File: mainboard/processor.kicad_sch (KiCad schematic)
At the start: 83 parts, among them J10 6502, J11 6502, J12 Y, J13 Conn_01x16, J14 NO DMA, J3 EDAC 305-044-520-201, J4 W, J5 X, J6 S, J7 R, J8 T, J9 Z, Q1 Q_NPN_EBC, Q2 Q_PNP_EBC, Q3 Q_NPN_EBC, Q4 Q_PNP_EBC

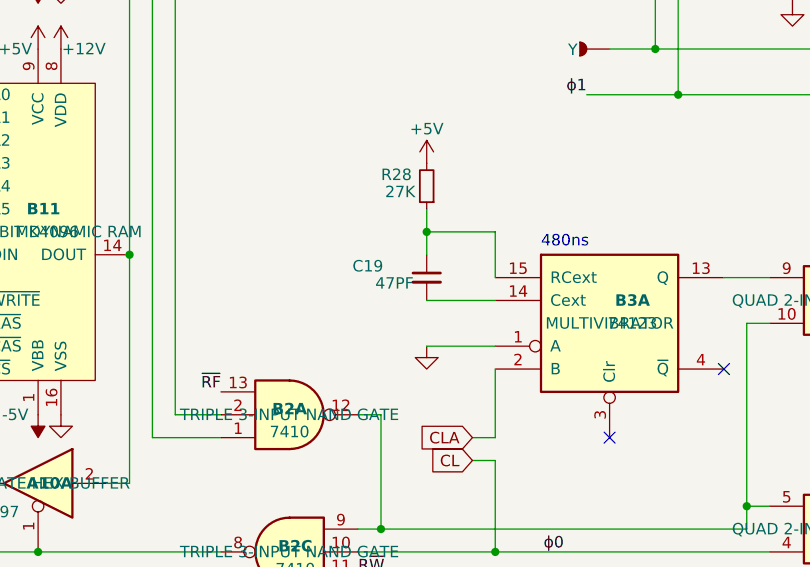
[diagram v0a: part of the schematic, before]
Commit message: added graphicard
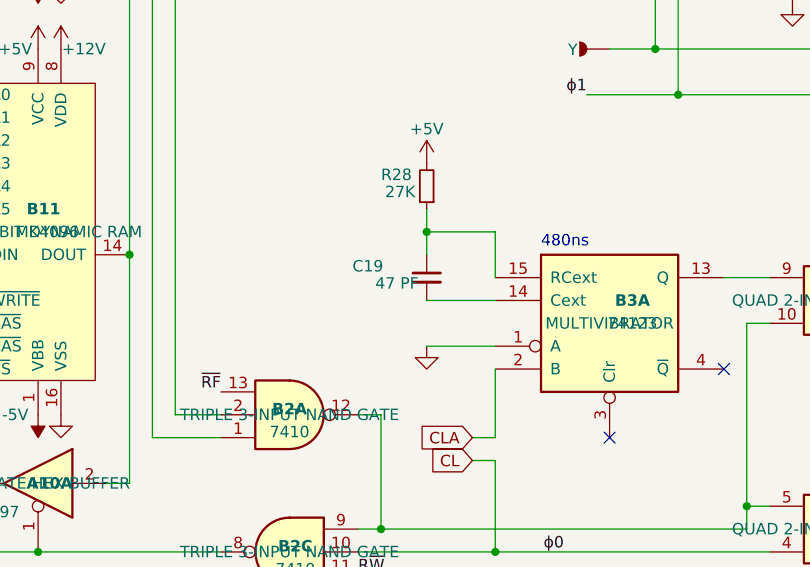
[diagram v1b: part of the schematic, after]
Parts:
- C19: value 47PF -> 47 PF
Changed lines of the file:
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@@
 			)
 		)
-		(property "Value" "47PF"
+		(property "Value" "47 PF"
 			(at 413.385 142.875 0)
 			(show_name no)

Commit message: mainboard work
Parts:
- C10, C11, C12, C13, C8, C9, R16, R17, R18, R19, R20, R21, R22, R23: now not fitted; now left out of the parts list
- C15, C16, C17, C18, C21, C22, C23, C24: footprint mainboard:apple-1_C_Disc_D16.0mm_W5.0mm_P7.50mm -> mainboard:apple-1_C_Disc_D16.0mm_W5.0mm_P275mils
- Q1, Q2, Q3, Q4: now not fitted
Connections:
- net at B3.14 (Cext): now also C19.1; no longer C19.2
- net at B3.15 (RCext), R28.1: now also C19.2; no longer C19.1
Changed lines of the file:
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@@
 		(body_style 1)
 		(exclude_from_sim no)
-		(in_bom yes)
+		(in_bom no)
 		(on_board yes)
 		(in_pos_files yes)
-		(dnp no)
+		(dnp yes)
 		(property "Reference" "C8"
 			(at 248.158 253.238 0)
@@
 		(body_style 1)
 		(exclude_from_sim no)
-		(in_bom yes)
+		(in_bom no)
 		(on_board yes)
 		(in_pos_files yes)
-		(dnp no)
+		(dnp yes)
 		(property "Reference" "C9"
 			(at 248.412 237.998 0)
@@
 		(body_style 1)
 		(exclude_from_sim no)
-		(in_bom yes)
+		(in_bom no)
 		(on_board yes)
 		(in_pos_files yes)
-		(dnp no)
+		(dnp yes)
 		(property "Reference" "R21"
 			(at 259.334 240.284 0)
@@
 		(body_style 1)
 		(exclude_from_sim no)
-		(in_bom yes)
+		(in_bom no)
 		(on_board yes)
 		(in_pos_files yes)
-		(dnp no)
+		(dnp yes)
 		(property "Reference" "R20"
 			(at 259.334 250.444 0)
@@
 		(body_style 1)
 		(exclude_from_sim no)
-		(in_bom yes)
+		(in_bom no)
 		(on_board yes)
 		(in_pos_files yes)
-		(dnp no)
+		(dnp yes)
 		(property "Reference" "R16"
 			(at 247.142 263.144 0)
@@
 		(body_style 1)
 		(exclude_from_sim no)
-		(in_bom yes)
+		(in_bom no)
 		(on_board yes)
 		(in_pos_files yes)
-		(dnp no)
+		(dnp yes)
 		(property "Reference" "R17"
 			(at 247.396 227.838 0)
@@
 		(body_style 1)
 		(exclude_from_sim no)
-		(in_bom yes)
+		(in_bom no)
 		(on_board yes)
 		(in_pos_files yes)
-		(dnp no)
+		(dnp yes)
 		(property "Reference" "C12"
 			(at 261.874 233.426 0)
@@
 		(on_board yes)
 		(in_pos_files yes)
-		(dnp no)
+		(dnp yes)
 		(property "Reference" "Q1"
 			(at 256.54 259.08 0)
@@
 		(on_board yes)
 		(in_pos_files yes)
-		(dnp no)
+		(dnp yes)
 		(property "Reference" "Q2"
 			(at 256.54 233.68 0)
@@
 		(lib_id "Device:C_Small")
 		(at 419.1 142.24 0)
+		(mirror x)
 		(unit 1)
 		(body_style 1)
@@
 		(dnp no)
 		(property "Reference" "C19"
-			(at 410.845 140.97 0)
+			(at 410.845 143.51 0)
 			(show_name no)
 			(do_not_autoplace no)
@@
 		)
 		(property "Value" "47 PF"
-			(at 413.385 142.875 0)
+			(at 413.385 141.605 0)
 			(show_name no)
 			(do_not_autoplace no)
@@
 		(body_style 1)
 		(exclude_from_sim no)
-		(in_bom yes)
+		(in_bom no)
 		(on_board yes)
 		(in_pos_files yes)
-		(dnp no)
+		(dnp yes)
 		(property "Reference" "C10"
 			(at 248.158 303.53 0)
@@
 		(body_style 1)
 		(exclude_from_sim no)
-		(in_bom yes)
+		(in_bom no)
 		(on_board yes)
 		(in_pos_files yes)
-		(dnp no)
+		(dnp yes)
 		(property "Reference" "C11"
 			(at 247.904 288.798 0)
@@
 		(body_style 1)
 		(exclude_from_sim no)
-		(in_bom yes)
+		(in_bom no)
 		(on_board yes)
 		(in_pos_files yes)
-		(dnp no)
+		(dnp yes)
 		(property "Reference" "R23"
 			(at 259.334 291.338 0)
@@
 		(body_style 1)
 		(exclude_from_sim no)
-		(in_bom yes)
+		(in_bom no)
 		(on_board yes)
 		(in_pos_files yes)
-		(dnp no)
+		(dnp yes)
 		(property "Reference" "R22"
 			(at 259.334 301.244 0)
@@
 		(body_style 1)
 		(exclude_from_sim no)
-		(in_bom yes)
+		(in_bom no)
 		(on_board yes)
 		(in_pos_files yes)
-		(dnp no)
+		(dnp yes)
 		(property "Reference" "R18"
 			(at 247.142 313.944 0)
@@
 		(body_style 1)
 		(exclude_from_sim no)
-		(in_bom yes)
+		(in_bom no)
 		(on_board yes)
 		(in_pos_files yes)
-		(dnp no)
+		(dnp yes)
 		(property "Reference" "R19"
 			(at 247.142 278.892 0)
@@
 		(body_style 1)
 		(exclude_from_sim no)
-		(in_bom yes)
+		(in_bom no)
 		(on_board yes)
 		(in_pos_files yes)
-		(dnp no)
+		(dnp yes)
 		(property "Reference" "C13"
 			(at 261.874 283.718 0)
@@
 		(on_board yes)
 		(in_pos_files yes)
-		(dnp no)
+		(dnp yes)
 		(property "Reference" "Q3"
 			(at 256.54 309.88 0)
@@
 		(on_board yes)
 		(in_pos_files yes)
-		(dnp no)
+		(dnp yes)
 		(property "Reference" "Q4"
 			(at 256.54 284.48 0)
@@
 			)
 		)
-		(property "Footprint" "mainboard:apple-1_C_Disc_D16.0mm_W5.0mm_P7.50mm"
+		(property "Footprint" "mainboard:apple-1_C_Disc_D16.0mm_W5.0mm_P275mils"
 			(at 27.94 99.06 0)
 			(hide yes)
@@
 			)
 		)
-		(property "Footprint" "mainboard:apple-1_C_Disc_D16.0mm_W5.0mm_P7.50mm"
+		(property "Footprint" "mainboard:apple-1_C_Disc_D16.0mm_W5.0mm_P275mils"
 			(at 35.56 99.06 0)
 			(hide yes)
@@
 			)
 		)
-		(property "Footprint" "mainboard:apple-1_C_Disc_D16.0mm_W5.0mm_P7.50mm"
+		(property "Footprint" "mainboard:apple-1_C_Disc_D16.0mm_W5.0mm_P275mils"
 			(at 43.18 99.06 0)
 			(hide yes)
@@
 			)
 		)
-		(property "Footprint" "mainboard:apple-1_C_Disc_D16.0mm_W5.0mm_P7.50mm"
+		(property "Footprint" "mainboard:apple-1_C_Disc_D16.0mm_W5.0mm_P275mils"
 			(at 50.8 99.06 0)
 			(hide yes)
@@
 			)
 		)
-		(property "Footprint" "mainboard:apple-1_C_Disc_D16.0mm_W5.0mm_P7.50mm"
+		(property "Footprint" "mainboard:apple-1_C_Disc_D16.0mm_W5.0mm_P275mils"
 			(at 27.94 116.84 0)
 			(hide yes)
@@
 			)
 		)
-		(property "Footprint" "mainboard:apple-1_C_Disc_D16.0mm_W5.0mm_P7.50mm"
+		(property "Footprint" "mainboard:apple-1_C_Disc_D16.0mm_W5.0mm_P275mils"
 			(at 35.56 116.84 0)
 			(hide yes)
@@
 			)
 		)
-		(property "Footprint" "mainboard:apple-1_C_Disc_D16.0mm_W5.0mm_P7.50mm"
+		(property "Footprint" "mainboard:apple-1_C_Disc_D16.0mm_W5.0mm_P275mils"
 			(at 43.18 116.84 0)
 			(hide yes)
@@
 			)
 		)
-		(property "Footprint" "mainboard:apple-1_C_Disc_D16.0mm_W5.0mm_P7.50mm"
+		(property "Footprint" "mainboard:apple-1_C_Disc_D16.0mm_W5.0mm_P275mils"
 			(at 50.8 116.84 0)
 			(hide yes)

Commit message: added kicad drawing template
new file:   boardfont.svg
new file:   img/00101P3.png
new file:   mainboard/apple1template.kicad_wks
additional work on mainboard
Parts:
- added C25, C26, C27, C28, C29, C30: 1.0u, mainboard:apple-1_C_Disc_D16.0mm_W5.0mm_P7.50mm, symbol Device:CP1_Small
- JP1: footprint (none) -> mainboard:apple-1_KBD-IRQ
- JP2: footprint (none) -> mainboard:apple-1_DSP-NMI
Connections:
- net +5V: now also C25.1, C26.1, C27.1, C28.1, C29.1, C30.1
- net GND: now also C25.2, C26.2, C27.2, C28.2, C29.2, C30.2
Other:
- note added: "NOTES: (continued from sheet 1/3) 7. UNIT, AS SUPPLIED, IN- CLUDES A 6502 MICRO- PROCESSOR, AND SOLDER JUMPERS AT BOTH POINTS MARKED "6502", AND HAS OMITTED ALL COMPON- ENTS SHOWN WITHIN THE DOTTED BOX. IF A 6800 IS SUBSTITUTED FOR THE 6502 IT IS NECESSARY TO INSTALL ALL COMPON- ENTS SHOWN, AND TO BREAK BOTH SOLDER BRIDGES NOTED "6502". 8. UNIT IS SUPPLIED WITH : Y JUMPERED TO CSF Z JUMPERED TO C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"
- note removed: "UNIT IS SUPPLIED WITH : Y JUMPERED TO CSF Z JUMPERED TO CSD W JUMPERED TO CS1 X JUMPERED TO CS0 R, S AND T ARE USER SELECTABLE CHIP SELECTS. (4K BLOCKS)"

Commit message: board is now complete, cleanup work can begin
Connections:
- net +5V: now also C25.2, C26.2, C27.2, C28.2, C29.2, C30.2; no longer C25.1, C26.1, C27.1, C28.1, C29.1, C30.1
- net GND: now also C25.1, C26.1, C27.1, C28.1, C29.1, C30.1; no longer C25.2, C26.2, C27.2, C28.2, C29.2, C30.2
- net at A11.13 (~{CS}), A12.13 (~{CS}), A13.13 (~{CS})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: now also J4.20; no longer J4.1
- net at J3.11: now also J6.18; no longer J6.1
- net at J3.L: now also J8.19; no longer J8.1
- net at A4.23 (~{CS2}): now also J9.23; no longer J9.1
- net at B11.13 (~{CS}), B12.13 (~{CS}), B13.13 (~{CS})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: now also J5.21; no longer J5.1
- net at A1.13 (~{CS1}), A2.13 (~{CS1}): now also J12.22; no longer J12.1
- net at B3.7 (RCext), C20.1: now also R29.1
- net at B3.6 (Cext), C20.2: no longer R29.1
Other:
- moved on the sheet: R29
